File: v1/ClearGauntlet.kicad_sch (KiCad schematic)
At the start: 1 part

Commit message: Schematics
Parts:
- added Index, Index_Splay, Middle, Middle_Splay, Pink_Splay, Pinky, Ring, Ring_Splay, Thumb, Thumb_Splay: 10k Potentiometer, symbol Device:R_Potentiometer
- added J?: USB_B_Micro, symbol Connector:USB_B_Micro
- added M? (x5): Motor_Servo, symbol Motor:Motor_Servo
- added SW1, SW2: SW_Push, symbol Switch:SW_Push
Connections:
- net at U?.10 (D19): now also Index_Splay.2
- net at U?.11 (D21): now also Thumb_Splay.2
- net at U?.19 (D34): now also M?.1 (PWM)
- net GND: now reaches U?.2 (GND), U?.29 (GND)
- net GND: now also Index.3, Index_Splay.3, J?.5 (GND), M?.3 (-), M?.3 (-), M?.3 (-), M?.3 (-), M?.3 (-), Middle.3, Middle_Splay.3, Pink_Splay.3, Pinky.3, Ring.3, Ring_Splay.3, SW1.2, SW2.2, Thumb.3, Thumb_Splay.3
- net at U?.20 (D35): now also M?.1 (PWM)
- net at U?.21 (D32): now also M?.1 (PWM)
- net at U?.22 (D33): now also M?.1 (PWM)
- net at U?.25 (D27): now also M?.1 (PWM)
- net at U?.26 (D14): now also Pink_Splay.2
- net at U?.27 (D12): now also Index.2
- net at U?.28 (D13): now also Thumb.2
- net at U?.3 (D15): now also Ring_Splay.2
- net at U?.30 (VIN): now also Index.1, Index_Splay.1, Middle.1, Middle_Splay.1, Pink_Splay.1, Pinky.1, Ring.1, Ring_Splay.1, SW1.1, SW2.1, Thumb.1, Thumb_Splay.1
- net at U?.4 (D2): now also Pinky.2
- net at U?.5 (D4): now also Ring.2
- net at U?.8 (D5): now also Middle.2
- net at U?.9 (D18): now also Middle_Splay.2
- new net: J?.1 (VBUS), M?.2 (+), M?.2 (+), M?.2 (+), M?.2 (+), M?.2 (+)
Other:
- note added: "ClearGauntlet V1"
- note added: "D34, D35, D32, D33, D25, D26, D27, D14, D12, D13, D4, D2, D15 --- ADC"
- note added: "ESP32 - DEVKITv1 10 potentiometers (5 for curl, 5 for splay) 5 servos 3.3V supply from ESP32 5V supply from battery (through micro-USB split)"

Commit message: adding PCB updated with schematics
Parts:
- removed J?: USB_B_Micro, symbol Connector:USB_B_Micro
- Index1: renamed from Index; footprint (none) -> Potentiometer_THT:Potentiometer_Bourns_3266Y_Vertical
- Index_Splay1: renamed from Index_Splay; footprint (none) -> Potentiometer_THT:Potentiometer_Bourns_3266Y_Vertical
- M1, M2, M3, M4, M5: renamed from M?; footprint (none) -> Potentiometer_THT:Potentiometer_Bourns_3266Y_Vertical
- Middle1: renamed from Middle; footprint (none) -> Potentiometer_THT:Potentiometer_Bourns_3266Y_Vertical
- Middle_Splay1: renamed from Middle_Splay; footprint (none) -> Potentiometer_THT:Potentiometer_Bourns_3266Y_Vertical
- Pink_Splay1: renamed from Pink_Splay; footprint (none) -> Potentiometer_THT:Potentiometer_Bourns_3266Y_Vertical
- Pinky1: renamed from Pinky; footprint (none) -> Potentiometer_THT:Potentiometer_Bourns_3266Y_Vertical
- Ring1: renamed from Ring; footprint (none) -> Potentiometer_THT:Potentiometer_Bourns_3266Y_Vertical
- Ring_Splay1: renamed from Ring_Splay; footprint (none) -> Potentiometer_THT:Potentiometer_Bourns_3266Y_Vertical
- SW1, SW2: footprint (none) -> Button_Switch_SMD:SW_Push_SPST_NO_Alps_SKRK
- Thumb1: renamed from Thumb; footprint (none) -> Potentiometer_THT:Potentiometer_Bourns_3266Y_Vertical
- Thumb_Splay1: renamed from Thumb_Splay; footprint (none) -> Potentiometer_THT:Potentiometer_Bourns_3266Y_Vertical
- U1: renamed from U?; footprint MODULE_ESP32_DEVKIT_V1 -> ESP32-DEVKIT-V1:MODULE_ESP32_DEVKIT_V1
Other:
- note added: "Power bank (5V)"

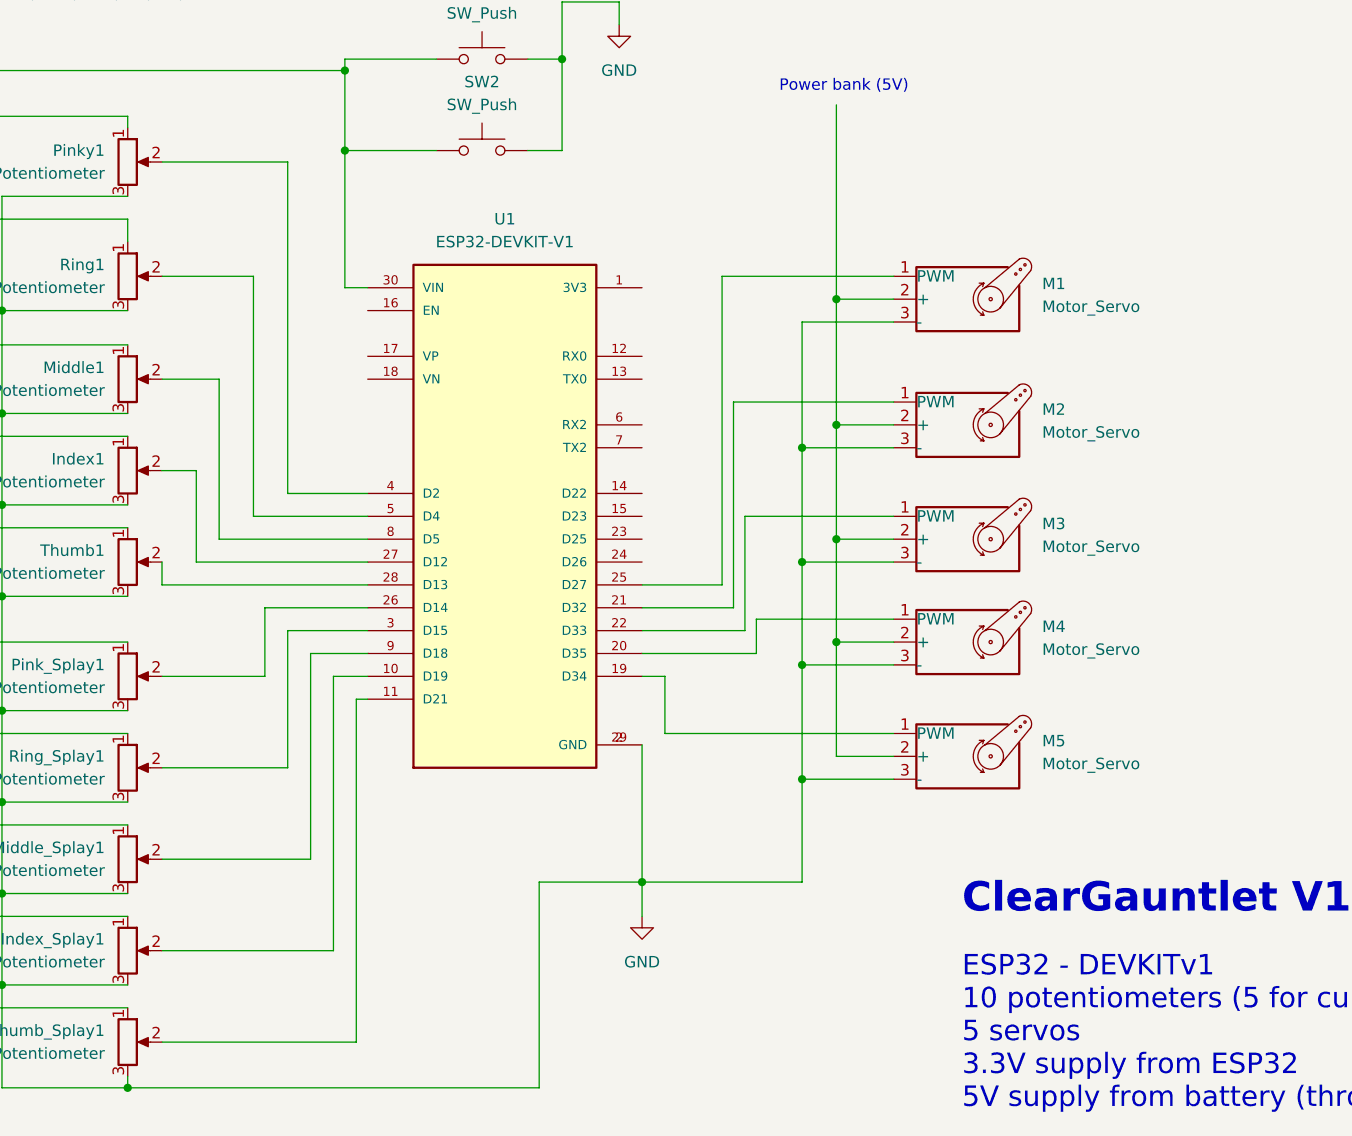
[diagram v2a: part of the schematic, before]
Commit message: PCB with wiring
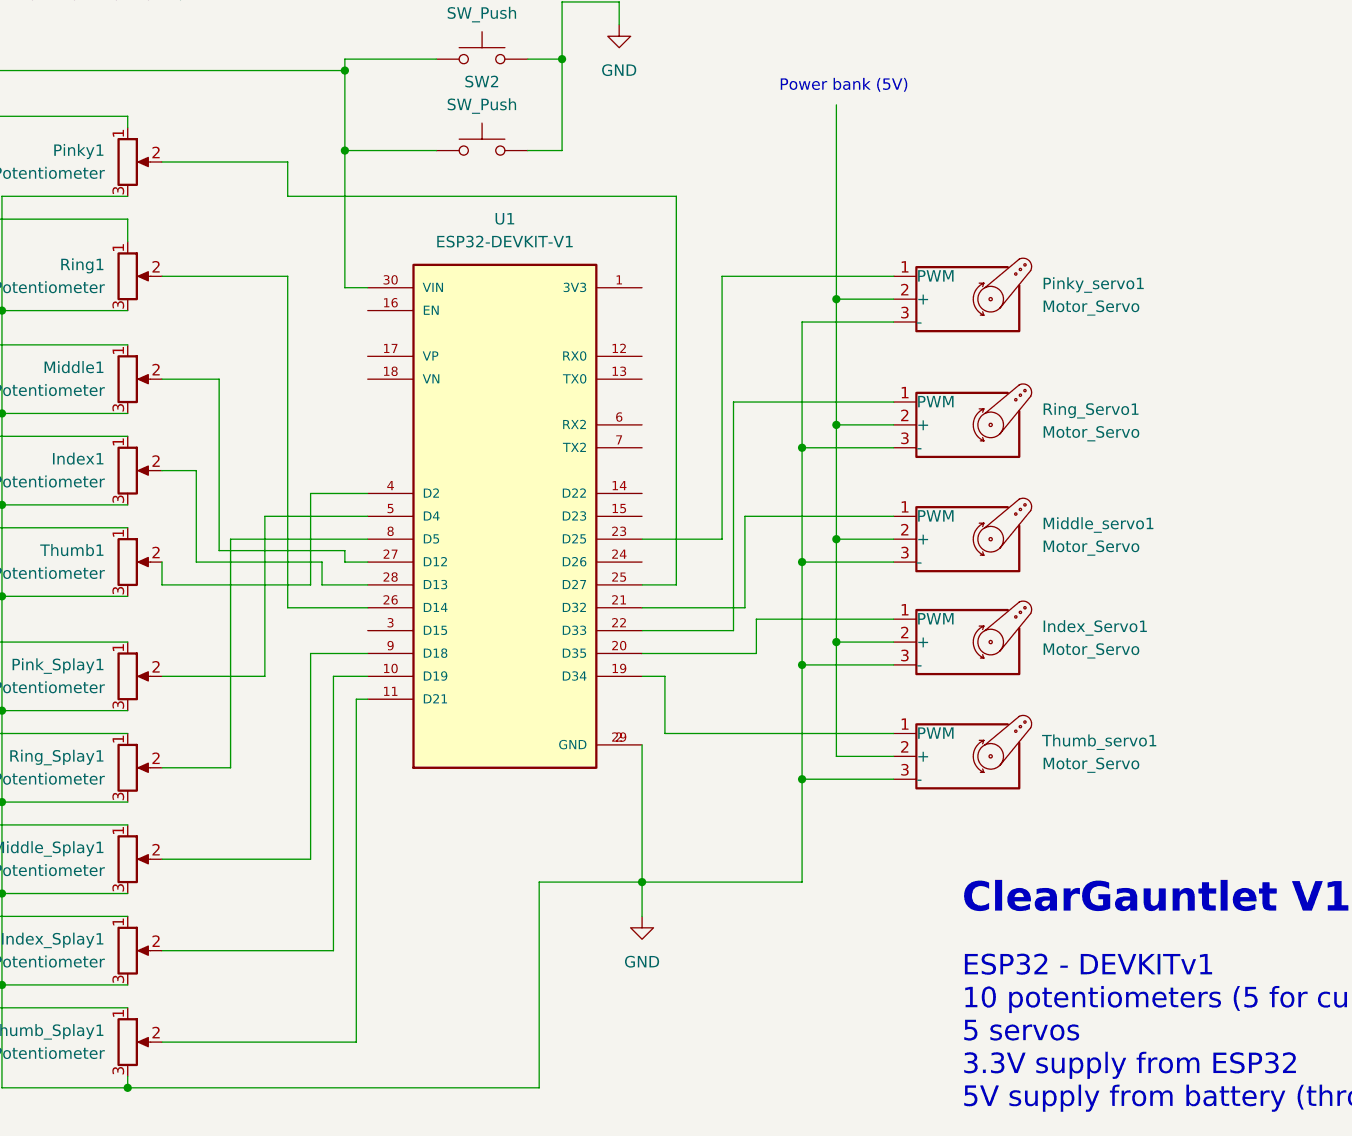
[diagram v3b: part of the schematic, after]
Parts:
- renumbered M4 to Index_Servo1, M3 to Middle_servo1, M1 to Pinky_servo1, M2 to Ring_Servo1, M5 to Thumb_servo1
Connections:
- net at Pink_Splay1.2: now also U1.5 (D4); no longer U1.26 (D14)
- net at Thumb1.2: now also U1.4 (D2); no longer U1.28 (D13)
- net at Index1.2: now also U1.28 (D13); no longer U1.27 (D12)
- net at Ring1.2: now also U1.26 (D14); no longer U1.5 (D4)
- net at Middle_servo1.1 (PWM): now also U1.21 (D32); no longer U1.22 (D33)
- net at Pinky_servo1.1 (PWM): now also U1.23 (D25); no longer U1.25 (D27)
- net at Ring_Splay1.2: now also U1.8 (D5); no longer U1.3 (D15)
- net at Ring_Servo1.1 (PWM): now also U1.22 (D33); no longer U1.21 (D32)
- net at Pinky1.2: now also U1.25 (D27); no longer U1.4 (D2)
- net at Middle1.2: now also U1.27 (D12); no longer U1.8 (D5)

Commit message: adding v3
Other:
- note added: "#define PIN_PINKY 36 - D23 #define PIN_RING 39 - D22 #define PIN_MIDDLE 34 - D5 #define PIN_INDEX 35 - D18 #define PIN_THUMB 32 - #define PIN_JOY_X 33 #define PIN_JOY_Y 25 #define PIN_JOY_BTN 26 #define PIN_A_BTN 27 #define PIN_B_BTN 14 #define PIN_TRIG_BTN 12 //unused if gesture set #define PIN_GRAB_BTN 13 //unused if gesture set #define PIN_PNCH_BTN 23 //unused if gesture set #define PIN_CALIB 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"
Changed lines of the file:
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@@
     (effects (font (size 2.27 2.27)) (justify left bottom))
+  )
+  (text "  #define PIN_PINKY     36 - D23\n  #define PIN_RING      39 - D22\n  #define PIN_MIDDLE    34 - D5\n  #define PIN_INDEX     35 - D18\n  #define PIN_THUMB     32 - \n  #define PIN_JOY_X     33\n  #define PIN_JOY_Y     25\n  #define PIN_JOY_BTN   26\n  #define PIN_A_BTN     27 \n  #define PIN_B_BTN     14\n  #define PIN_TRIG_BTN  12 //unused if gesture set\n  #define PIN_GRAB_BTN  13 //unused if gesture set\n  #define PIN_PNCH_BTN  23 //unused if gesture set\n  #define PIN_CALIB     12 //button for recalibration (You can set this to GPIO0 to use the BOOT button, but only when using Bluetooth.)\n  #define DEBUG_LED 2\n  #define PIN_PINKY_MOTOR     5  //used for force feedback\n  #define PIN_RING_MOTOR      18 //^\n  #define PIN_MIDDLE_MOTOR    19 //^\n  #define PIN_INDEX_MOTOR     21 //^\n  #define PIN_THUMB_MOTOR     17 //^\n  #define PIN_MENU_BTN        "
+    (at 17.78 190.5 0)
+    (effects (font (size 1.27 1.27)) (justify left bottom))
   )
   (text "Power bank (5V)" (at 171.45 40.64 0)
